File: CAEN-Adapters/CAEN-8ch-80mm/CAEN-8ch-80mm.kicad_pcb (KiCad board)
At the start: 2 copper layers, 80 x 80 mm, 10 parts

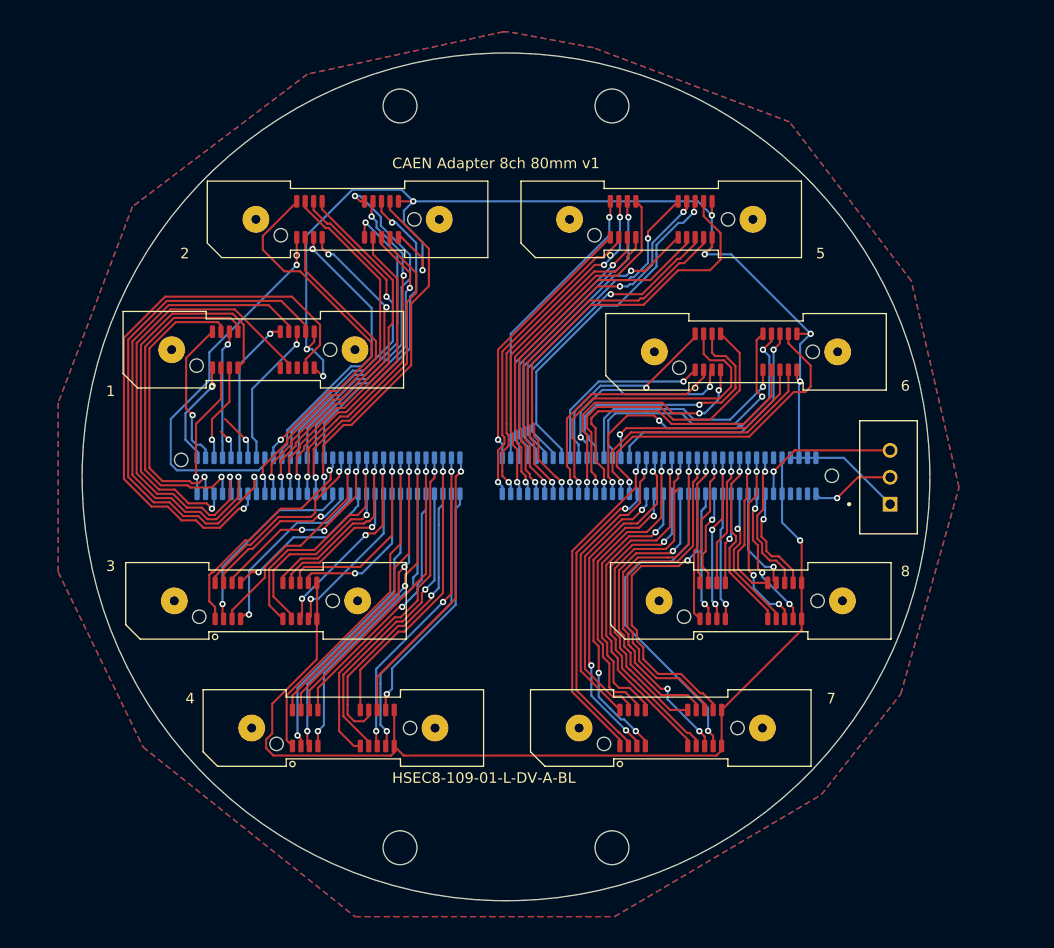
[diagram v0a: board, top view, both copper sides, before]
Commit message: Fixed CAEN-8ch-80mm disconnected traces
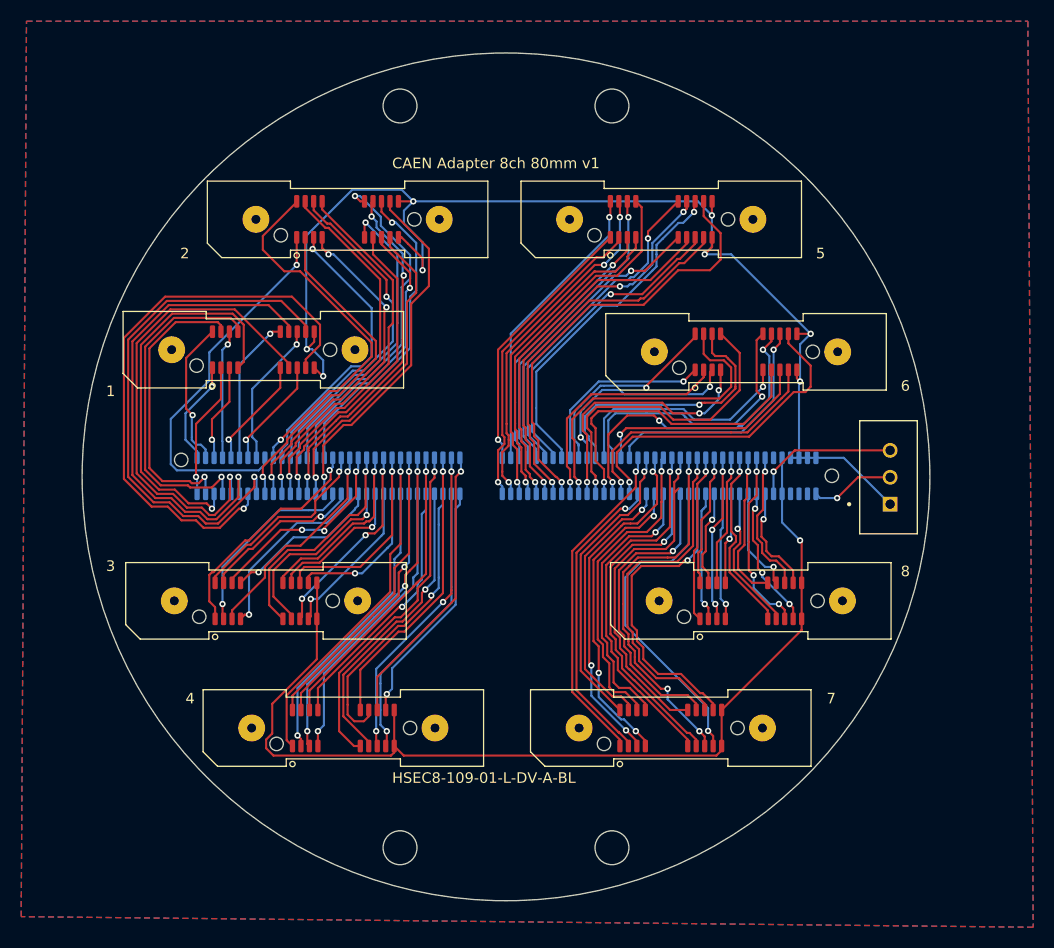
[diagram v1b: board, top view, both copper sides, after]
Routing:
- net A4: track 2.87 -> 10.6 mm
- net A6: track 4.57 -> 10.6 mm
- added copper zone on B.Cu, net (none)
- added copper zone on F.Cu, net (none)
- removed copper zone on B.Cu, net GND
- removed copper zone on F.Cu, net GND
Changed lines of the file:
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@@
 	)
 	(segment
-		(start 137.074678 81.477588)
-		(end 136.328 80.73091)
+		(start 141.95 74.7)
+		(end 141.95 76.602266)
+		(width 0.2)
+		(layer "F.Cu")
+		(net 11)
+	)
+	(segment
+		(start 141.95 76.602266)
+		(end 137.074678 81.477588)
 		(width 0.2)
 		(layer "F.Cu")
@@
 	)
 	(segment
-		(start 138.7 81.5)
-		(end 136.729 79.529)
+		(start 143.55 76.65)
+		(end 138.7 81.5)
+		(width 0.2)
+		(layer "F.Cu")
+		(net 15)
+	)
+	(segment
+		(start 143.55 74.7)
+		(end 143.55 76.65)
 		(width 0.2)
 		(layer "F.Cu")
@@
 	)
 	(zone
-		(net 33)
-		(net_name "GND")
+		(net 0)
+		(net_name "")
 		(layers "F.Cu" "B.Cu")
 		(hatch edge 0.5)
@@
 			(thermal_gap 0.5)
 			(thermal_bridge_width 0.5)
+			(island_removal_mode 1)
+			(island_area_min 10)
 		)
 		(polygon
 			(pts
-				(xy 163 43) (xy 144.5 47) (xy 128 59.5) (xy 121 78) (xy 121 94) (xy 129 110.5) (xy 149 126.5) (xy 173.5 126.5)
-				(xy 193 115) (xy 200.5 105.5) (xy 206 86) (xy 201.5 66.5) (xy 190 51.5) (xy 171.5 44.5) (xy 163.5 43)
+				(xy 118 42) (xy 212.5 42) (xy 213 127.5) (xy 117.5 126.5)
 			)
 		)
